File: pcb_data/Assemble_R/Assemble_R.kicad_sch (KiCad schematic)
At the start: 93 parts, among them U1 XIAO-nRF52840

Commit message: complete to design pattern of board R
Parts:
- U1: footprint Seeed Studio XIAO Series Library:XIAO-nRF52840-DIP -> Module:MOUDLE14P-XIAO-DIP-SMD
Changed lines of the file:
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@@
 			)
 		)
-		(property "Footprint" "Seeed Studio XIAO Series Library:XIAO-nRF52840-DIP"
+		(property "Footprint" "Module:MOUDLE14P-XIAO-DIP-SMD"
 			(at 232.41 80.264 0)
 			(effects

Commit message: update foot print reference, and fix GND filling area DRC error
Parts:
- U1: footprint Module:MOUDLE14P-XIAO-DIP-SMD -> Seeed Studio XIAO Series Library:XIAO-nRF52840-DIP
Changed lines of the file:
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@@
 			)
 		)
-		(property "Footprint" "Module:MOUDLE14P-XIAO-DIP-SMD"
+		(property "Footprint" "Seeed Studio XIAO Series Library:XIAO-nRF52840-DIP"
 			(at 232.41 80.264 0)
 			(effects

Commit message: replace footprint of xiao-nrf52840
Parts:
- U1: footprint Seeed Studio XIAO Series Library:XIAO-nRF52840-DIP -> mcu:xiao-ble-smd-cutout
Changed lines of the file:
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@@
 			)
 		)
-		(property "Footprint" "Seeed Studio XIAO Series Library:XIAO-nRF52840-DIP"
+		(property "Footprint" "mcu:xiao-ble-smd-cutout"
 			(at 232.41 80.264 0)
 			(effects

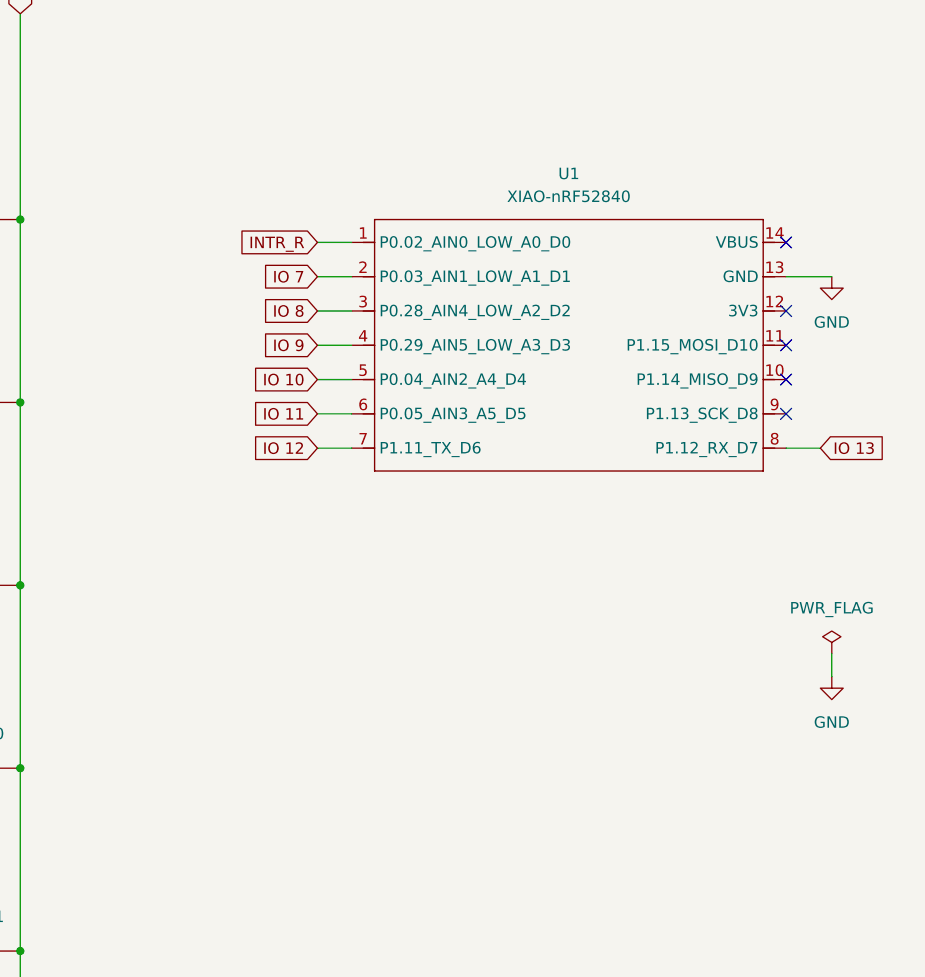
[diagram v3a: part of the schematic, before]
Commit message: replace symbol of xiao-ble
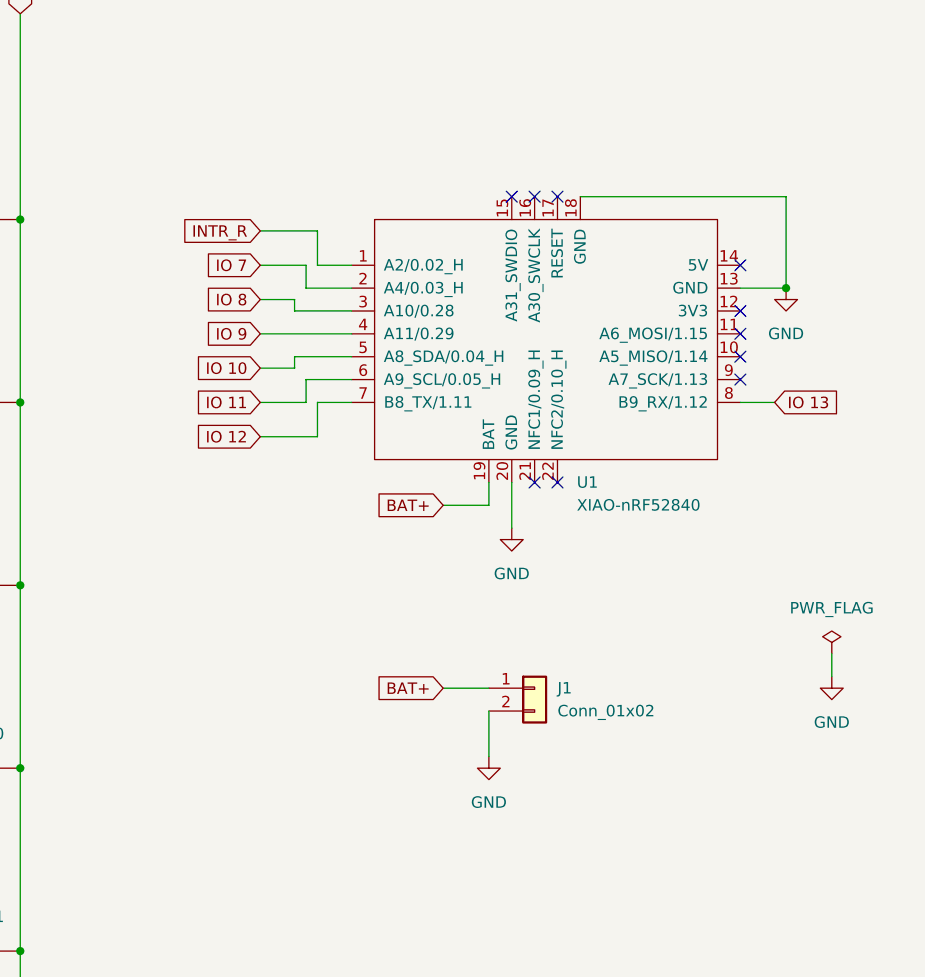
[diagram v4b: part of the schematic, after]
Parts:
- added J1: Conn_01x02, Connector_JST:JST_PH_B2B-PH-K_1x02_P2.00mm_Vertical, symbol Connector_Generic:Conn_01x02
- U1: symbol Seeed_Studio_XIAO_Series:XIAO-nRF52840-DIP -> mcu:xiao-ble
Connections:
- net GND: now also U1.18 (GND), U1.20 (GND), J1.2 (Pin_2)
- new net BAT+: J1.1 (Pin_1), U1.19 (BAT)
- no-connect marks 5 -> 10
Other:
- moved on the sheet: U1
